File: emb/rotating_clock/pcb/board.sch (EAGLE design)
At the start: 44 parts, among them IC1 CAT4016, IC2 CAT4016

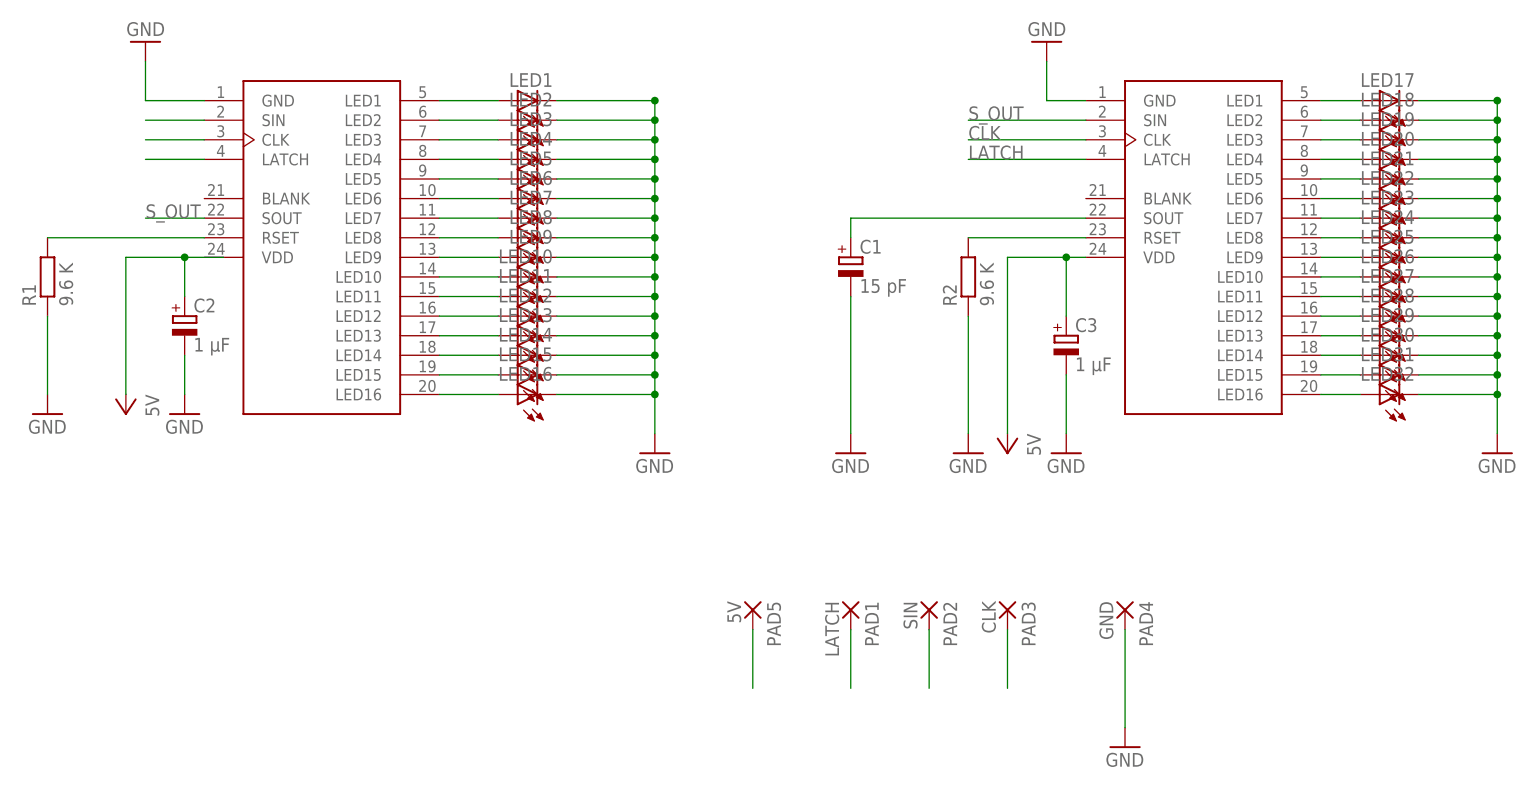
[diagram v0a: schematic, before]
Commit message: added slip ring board
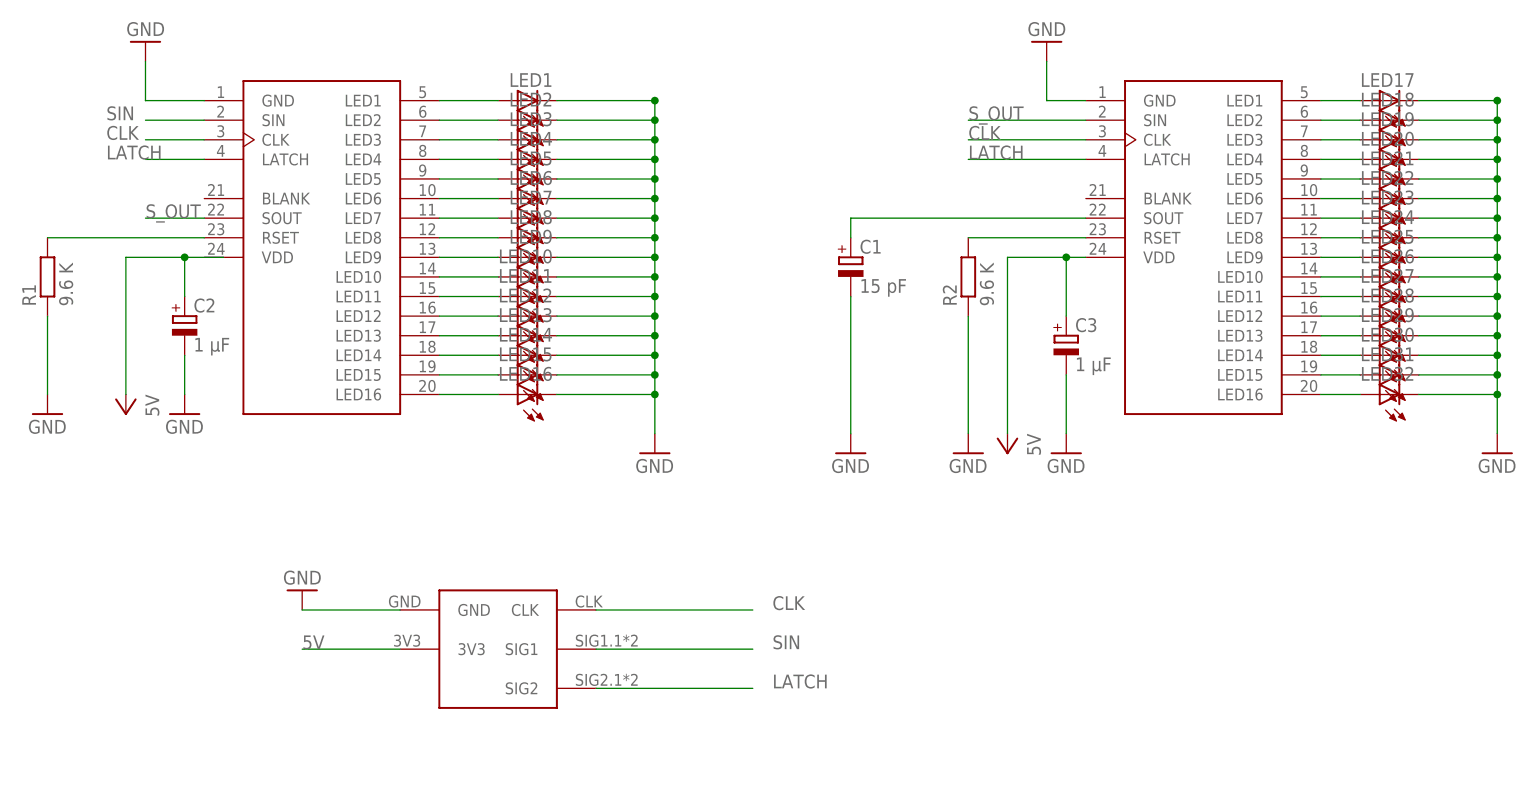
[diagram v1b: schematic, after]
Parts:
- removed PAD1: LATCH, wirepad:WIREPAD3,17/1,3
- removed PAD2: SIN, wirepad:WIREPAD3,17/1,3
- removed PAD3: CLK, wirepad:WIREPAD3,17/1,3
- removed PAD4: GND, wirepad:WIREPAD3,17/1,3
- removed PAD5: 5V, wirepad:WIREPAD3,17/1,3
- added U$1: SLIP-RING-INVERSE, slip_ring:SLIP-RING-INVERSE
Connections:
- net 5V: now also U$1.3V3; no longer PAD5.P
- net CLK: now also U$1.CLK; no longer PAD3.P
- net GND: now also U$1.GND; no longer PAD4.P
- net LATCH: now also U$1.SIG2; no longer PAD1.P
- net SIN: now also U$1.SIG1; no longer PAD2.P
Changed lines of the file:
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@@
 <?xml version="1.0" encoding="utf-8"?>
 <!DOCTYPE eagle SYSTEM "eagle.dtd">
-<eagle version="7.4.0">
+<eagle version="6.6.0">
 <drawing>
 <settings>
@@
 <part name="GND5" library="supply1" deviceset="GND" device=""/>
 <part name="GND6" library="supply1" deviceset="GND" device=""/>
-<part name="PAD1" library="wirepad" deviceset="WIREPAD" device="3,17/1,3" value="LATCH"/>
-<part name="PAD2" library="wirepad" deviceset="WIREPAD" device="3,17/1,3" value="SIN"/>
-<part name="PAD3" library="wirepad" deviceset="WIREPAD" device="3,17/1,3" value="CLK"/>
 <part name="C2" library="rcl" deviceset="CPOL-EU" device="E5-8.5" value="1 µF"/>
 <part name="C1" library="rcl" deviceset="CPOL-EU" device="E5-8.5" value="15 pF"/>
 <part name="GND7" library="supply1" deviceset="GND" device=""/>
 <part name="C3" library="rcl" deviceset="CPOL-EU" device="E5-8.5" value="1 µF"/>
-<part name="PAD4" library="wirepad" deviceset="WIREPAD" device="3,17/1,3" value="GND"/>
-<part name="PAD5" library="wirepad" deviceset="WIREPAD" device="3,17/1,3" value="5V"/>
 <part name="GND8" library="supply1" deviceset="GND" device=""/>
 <part name="GND9" library="supply1" deviceset="GND" device=""/>
 <part name="GND10" library="supply1" deviceset="GND" device=""/>
+<part name="U$1" library="slip_ring" deviceset="SLIP-RING-INVERSE" device=""/>
 </parts>
 <sheets>
@@
 <instance part="GND5" gate="1" x="58.42" y="43.18"/>
 <instance part="GND6" gate="1" x="167.64" y="43.18"/>
-<instance part="PAD1" gate="G$1" x="83.82" y="22.86" rot="R270"/>
-<instance part="PAD2" gate="G$1" x="93.98" y="22.86" rot="R270"/>
-<instance part="PAD3" gate="G$1" x="104.14" y="22.86" rot="R270"/>
 <instance part="C2" gate="G$1" x="-2.54" y="60.96"/>
 <instance part="C1" gate="G$1" x="83.82" y="68.58"/>
 <instance part="GND7" gate="1" x="83.82" y="43.18"/>
 <instance part="C3" gate="G$1" x="111.76" y="58.42"/>
-<instance part="PAD4" gate="G$1" x="119.38" y="22.86" rot="R270"/>
-<instance part="PAD5" gate="G$1" x="71.12" y="22.86" rot="R270"/>
-<instance part="GND8" gate="1" x="119.38" y="5.08"/>
+<instance part="GND8" gate="1" x="12.7" y="25.4" rot="R180"/>
 <instance part="GND9" gate="1" x="111.76" y="43.18"/>
 <instance part="GND10" gate="1" x="-2.54" y="48.26"/>
+<instance part="U$1" gate="G$1" x="38.1" y="12.7"/>
 </instances>
 <busses>
@@
 </segment>
 <segment>
-<pinref part="PAD4" gate="G$1" pin="P"/>
-<pinref part="GND8" gate="1" pin="GND"/>
-<wire x1="119.38" y1="20.32" x2="119.38" y2="7.62" width="0.1524" layer="91"/>
-</segment>
-<segment>
 <pinref part="C3" gate="G$1" pin="-"/>
 <pinref part="GND9" gate="1" pin="GND"/>
@@
 <wire x1="-2.54" y1="55.88" x2="-2.54" y2="50.8" width="0.1524" layer="91"/>
 </segment>
+<segment>
+<pinref part="U$1" gate="G$1" pin="GND"/>
+<pinref part="GND8" gate="1" pin="GND"/>
+<wire x1="12.7" y1="22.86" x2="25.4" y2="22.86" width="0.1524" layer="91"/>
+</segment>
 </net>
 <net name="5V" class="0">
 <segment>
-<pinref part="PAD5" gate="G$1" pin="P"/>
-<wire x1="71.12" y1="20.32" x2="71.12" y2="12.7" width="0.1524" layer="91"/>
+<wire x1="12.7" y1="17.78" x2="25.4" y2="17.78" width="0.1524" layer="91"/>
+<label x="12.7" y="17.78" size="1.778" layer="95"/>
+<pinref part="U$1" gate="G$1" pin="3V3"/>
 </segment>
 <segment>
@@
 </segment>
 <segment>
-<pinref part="PAD3" gate="G$1" pin="P"/>
-<wire x1="104.14" y1="20.32" x2="104.14" y2="12.7" width="0.1524" layer="91"/>
+<wire x1="71.12" y1="22.86" x2="50.8" y2="22.86" width="0.1524" layer="91"/>
+<label x="73.66" y="22.86" size="1.778" layer="95"/>
+<pinref part="U$1" gate="G$1" pin="CLK"/>
 </segment>
 <segment>
 <pinref part="IC1" gate="G$1" pin="CLK"/>
 <wire x1="0" y1="83.82" x2="-7.62" y2="83.82" width="0.1524" layer="91"/>
+<label x="-12.7" y="83.82" size="1.778" layer="95"/>
 </segment>
 </net>
@@
 </segment>
 <segment>
-<pinref part="PAD1" gate="G$1" pin="P"/>
-<wire x1="83.82" y1="20.32" x2="83.82" y2="12.7" width="0.1524" layer="91"/>
+<wire x1="71.12" y1="12.7" x2="50.8" y2="12.7" width="0.1524" layer="91"/>
+<label x="73.66" y="12.7" size="1.778" layer="95"/>
+<pinref part="U$1" gate="G$1" pin="SIG2"/>
 </segment>
 <segment>
 <pinref part="IC1" gate="G$1" pin="LATCH"/>
 <wire x1="0" y1="81.28" x2="-7.62" y2="81.28" width="0.1524" layer="91"/>
+<label x="-12.7" y="81.28" size="1.778" layer="95"/>
 </segment>
 </net>
@@
 <net name="SIN" class="0">
 <segment>
-<pinref part="PAD2" gate="G$1" pin="P"/>
-<wire x1="93.98" y1="20.32" x2="93.98" y2="12.7" width="0.1524" layer="91"/>
+<wire x1="71.12" y1="17.78" x2="50.8" y2="17.78" width="0.1524" layer="91"/>
+<label x="73.66" y="17.78" size="1.778" layer="95"/>
+<pinref part="U$1" gate="G$1" pin="SIG1"/>
 </segment>
 <segment>
 <pinref part="IC1" gate="G$1" pin="SIN"/>
 <wire x1="0" y1="86.36" x2="-7.62" y2="86.36" width="0.1524" layer="91"/>
-</segment>
-</net>
+<label x="-12.7" y="86.36" size="1.778" layer="95"/>
+</segment>
+</net>
